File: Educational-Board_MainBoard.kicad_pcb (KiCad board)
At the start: 2 copper layers, 155 x 75 mm, 215 parts, among them J201 Screw_Terminal_01x02_P5mm, J202 USB-C_304A-ACP16X, J401 ACC_INT1, J402 BME_SPI, J403 LUX_INT, J501 RGB_OUT, J601 PWR_IN1, J602 PWR_IN2, J603 PWR_IN3, J604 PWR_IN4, J605 MCP_INT, J606 5V, J607 GND, J608 3V3, J609 EX_PA, J610 EX_PB, J611 PWR_OUT1, J612 PWR_OUT3, J613 PWR_OUT2, J614 PWR_OUT4, Q501 AO3400A, Q601 IRLML9301TRPBF, Q602 IRLML9301TRPBF, Q603 IRLML9301TRPBF, Q604 IRLML9301TRPBF, SW301 RESET, SW501 BUTTON1, SW502 BUTTON2, SW503 BUTTON3, SW504 BUTTON4, SW505 BUTTON5, U201 TPS5430DDA, U202 NUCLEO64-H503RB, U401 LSM6DS3, U402 BME280, U403 OPT4001, U404 INA2180A2, U406 YK16S-L7.2-B10Ka(32-8)-G-A29, U501 74LVC1G34, U502 SSD1315 OLED 0.98", U601 TLP291-4, U602 TLP291-4, U603 MCP23017_SS

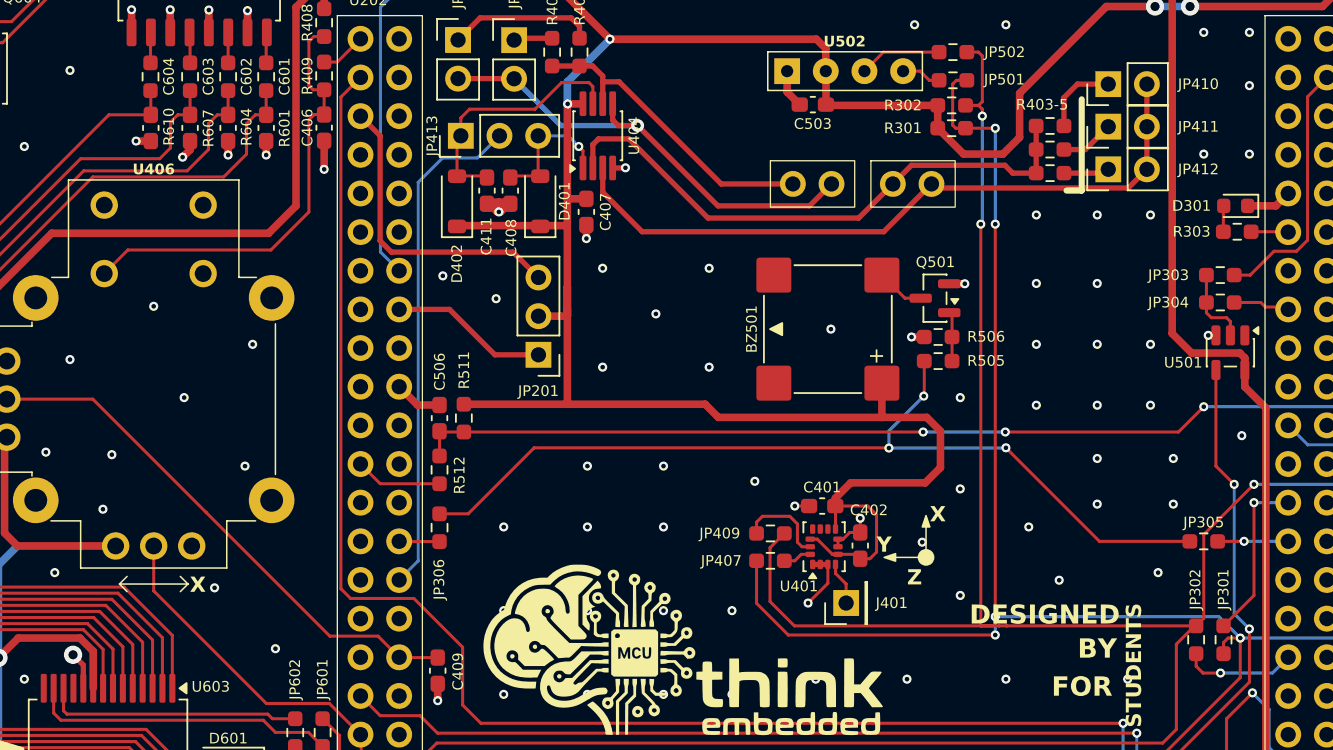
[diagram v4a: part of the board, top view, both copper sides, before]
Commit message: Added placeholders connectors for the Nucleo - TO ADD LCSC CODES
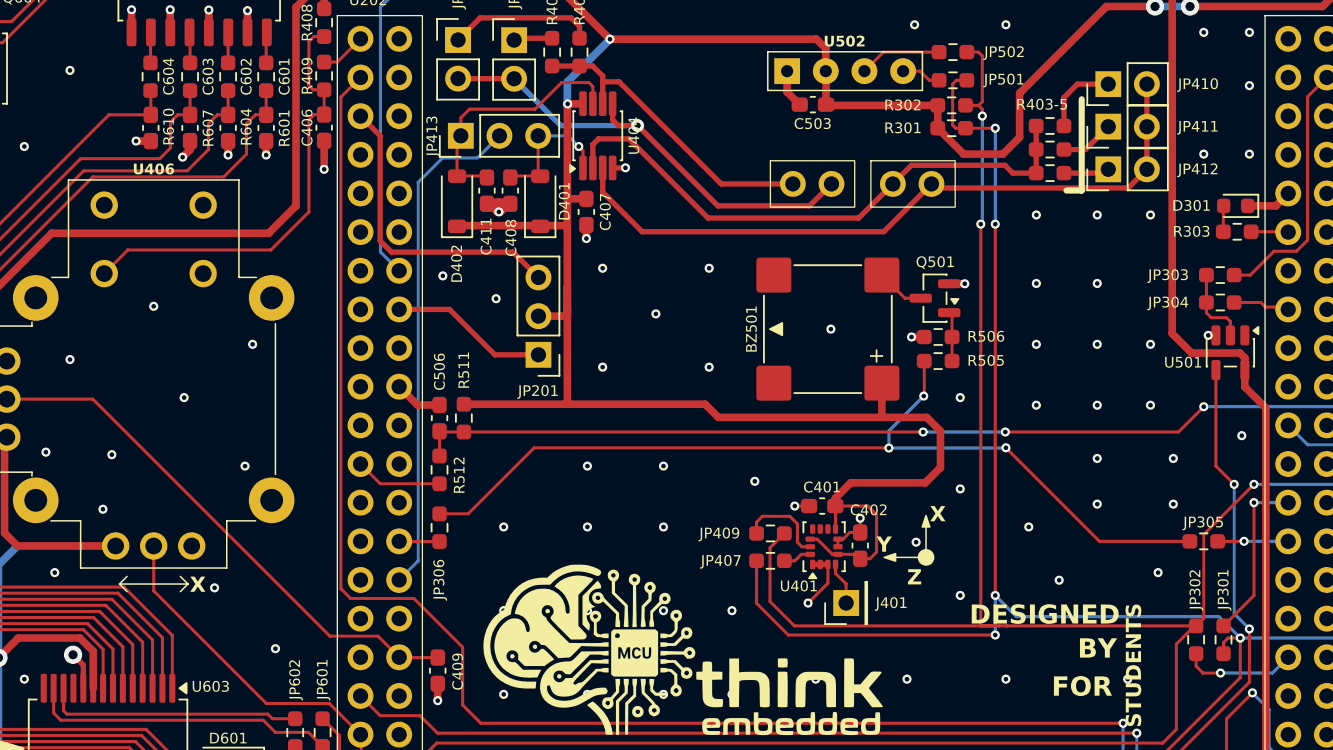
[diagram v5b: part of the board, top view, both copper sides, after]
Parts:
- added J301: Conn_02x20_Counter_Clockwise, ProjectConnectors:PLACEHOLDER_PinSocket_2x19_P2.54mm_Vertical, B.Cu at (118.6, 72.4)
- added J302: Conn_02x20_Counter_Clockwise, ProjectConnectors:PLACEHOLDER_PinSocket_2x19_P2.54mm_Vertical, B.Cu at (179.6, 72.4)
- added J303: Conn_01x02, ProjectConnectors:PLACEHOLDER_PinSocket_1x02_P2.54mm_Vertical, B.Cu at (147.0, 82.0)
- added J304: Conn_01x02, ProjectConnectors:PLACEHOLDER_PinSocket_1x02_P2.54mm_Vertical, B.Cu at (153.6, 82.0)
- added J305: Conn_02x05_Counter_Clockwise, ProjectConnectors:PLACEHOLDER_PinSocket_2x05_P2.54mm_Vertical, B.Cu at (171.9, 55.2)
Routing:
- net /MCU/I2C_SDA: track 251.5 -> 252.1 mm
